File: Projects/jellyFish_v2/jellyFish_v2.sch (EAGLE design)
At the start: 42 parts, among them P1 50, P2 50, P3 50, P4 50, P5 100, P6 100, P7 100, P8 100, Q1 IRF520, Q2 IRF520, Q3 IRF520, Q4 IRF520

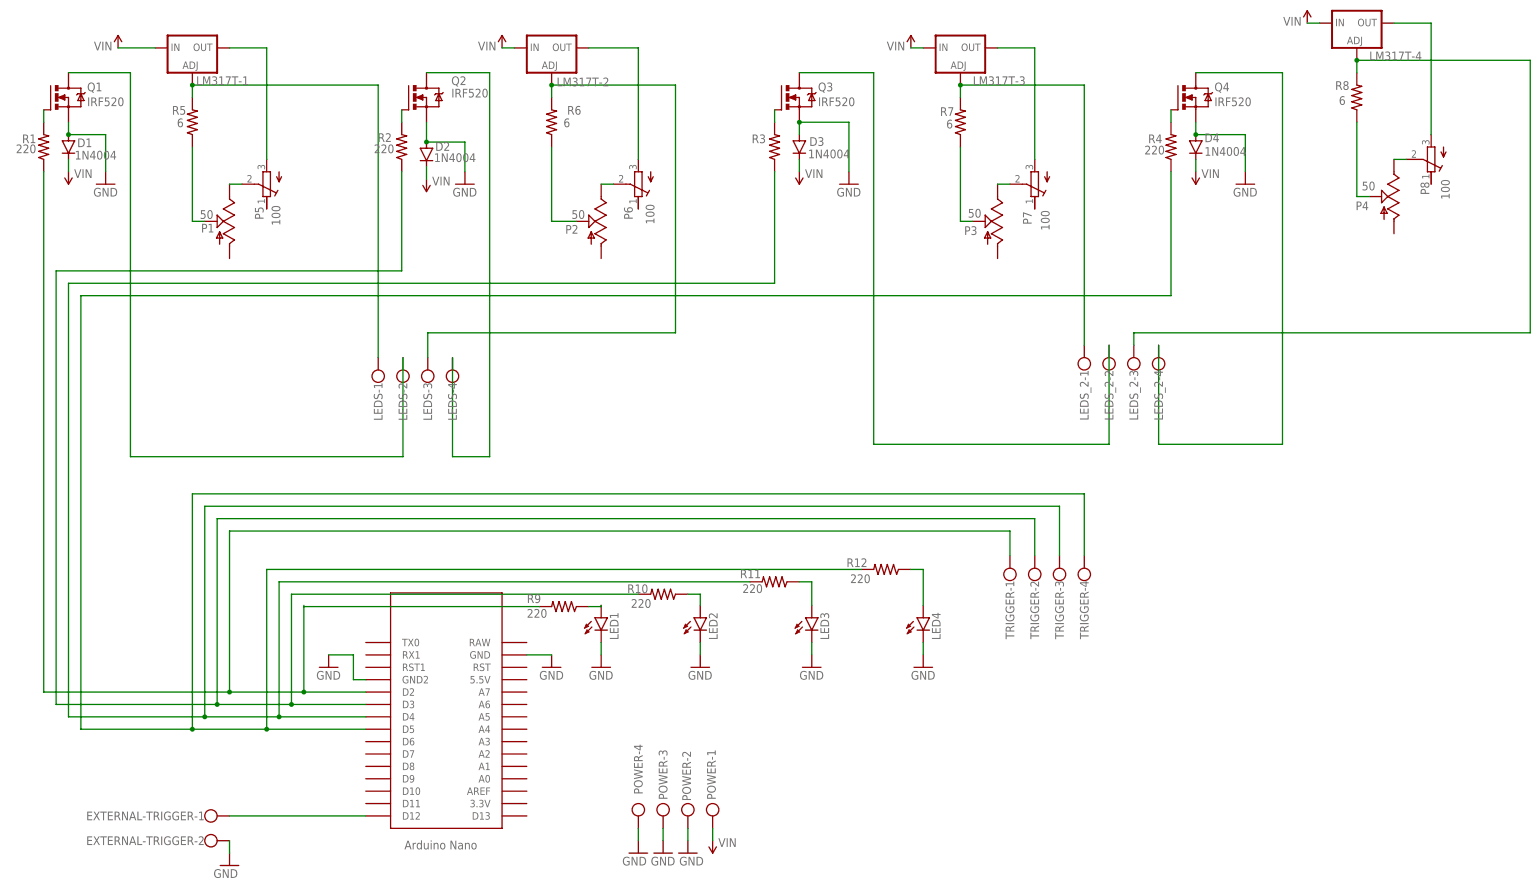
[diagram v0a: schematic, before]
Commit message: Added Trigger Outputs
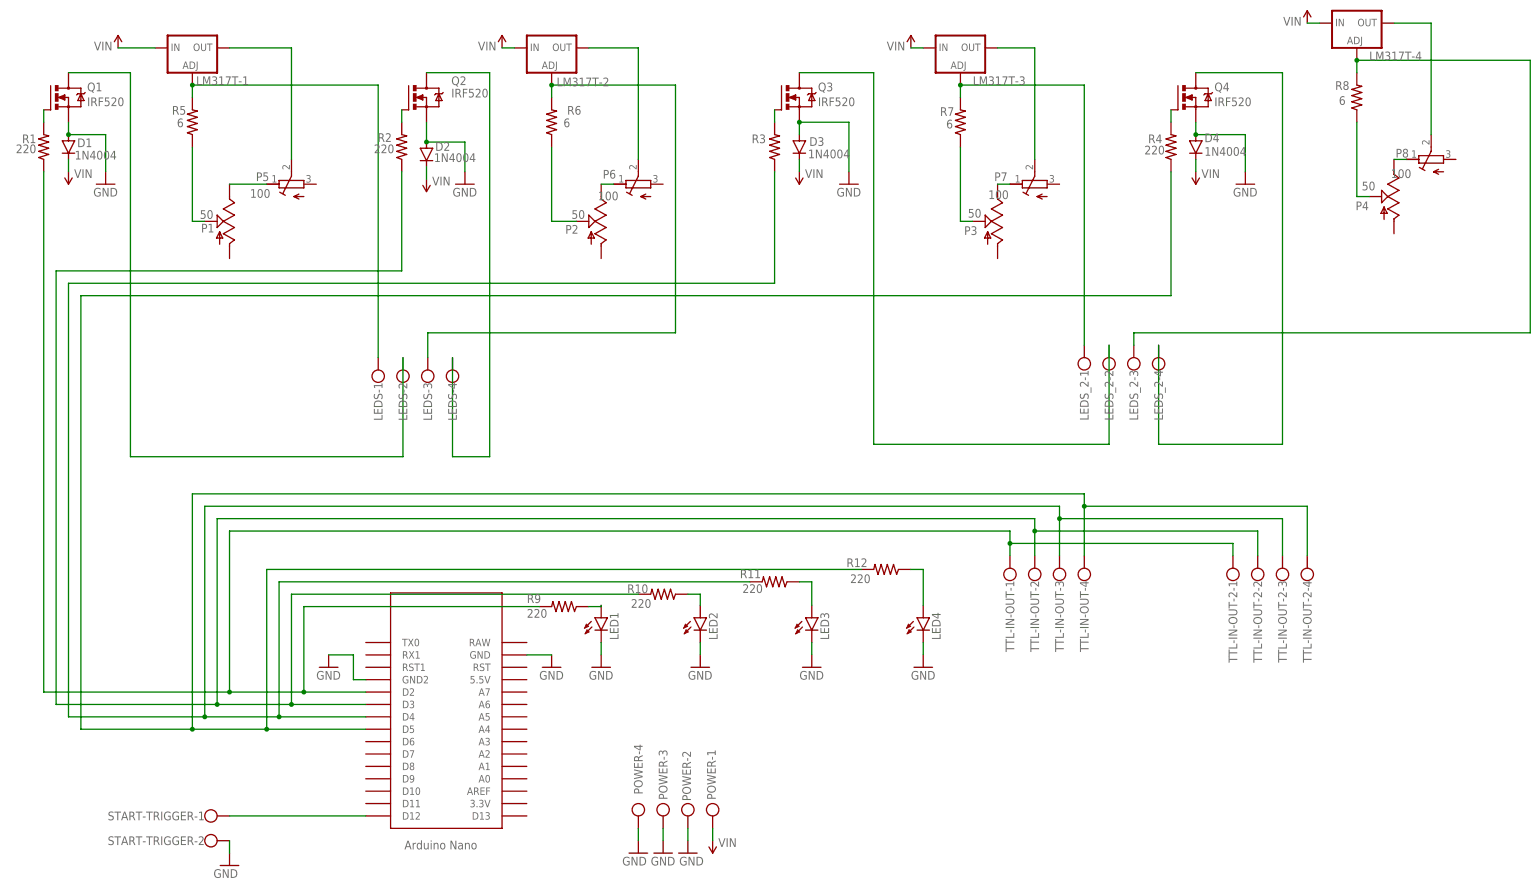
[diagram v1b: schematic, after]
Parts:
- added TTL-IN-OUT-2: (no value), con-wago-500:W237-4
- renumbered EXTERNAL-TRIGGER to START-TRIGGER, TRIGGER to TTL-IN-OUT
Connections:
- net N$1: now also P7.E; no longer P7.S
- net N$10: now also TTL-IN-OUT-2-3.KL
- net N$12: now also P4.E, P8.E; no longer LM317T-3.OUT, P7.A
- net N$14: now also LM317T-3.OUT, P7.S; no longer P4.E, P8.S
- net N$15: now also P5.E; no longer P5.S
- net N$18: now also P6.S; no longer P6.A
- net N$23: now also TTL-IN-OUT-2-4.KL
- net N$26: now also P8.S; no longer P8.A
- net N$27: now also P5.S; no longer P5.A
- net N$3: now also TTL-IN-OUT-2-1.KL
- net N$5: now also P6.E; no longer P6.S
- net N$6: now also TTL-IN-OUT-2-2.KL
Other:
- moved on the sheet: P5, P6, P7, P8
